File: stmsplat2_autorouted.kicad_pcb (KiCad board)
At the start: 2 copper layers, 100 x 100 mm, 113 parts, among them J1 C11_2X36, J10 Conn_01x03_Male, J11 Conn_01x02_Male, J12 Conn_01x04_Male, J13 Conn_01x04_Male, J14 Conn_01x02, J15 Conn_01x02, J16 Screw_Terminal_01x03, J17 Screw_Terminal_01x02, J2 C12_2X36, J3 Conn_01x04_Male, J4 Conn_01x04_Male, J5 Conn_Coaxial, J6 Conn_01x04_Male, J7 Conn_01x04_Male, J8 Conn_01x04_Male, J9 Conn_01x03_Male, Q1 BSS138LT1G, U1 ublox_chinese_PCB_module, U10 XCVR_E30-400M20S (Si4463), U11 3115_module, U2 ESP-C3-13U, U3 SST25VF032B, U4 48L512-48LM01, U5 Opamp_Quad_MCP6024, U6 E180-ZG120A, U7 AZ1084C, U8 MCP6S93-X_UN, U9 DS2485

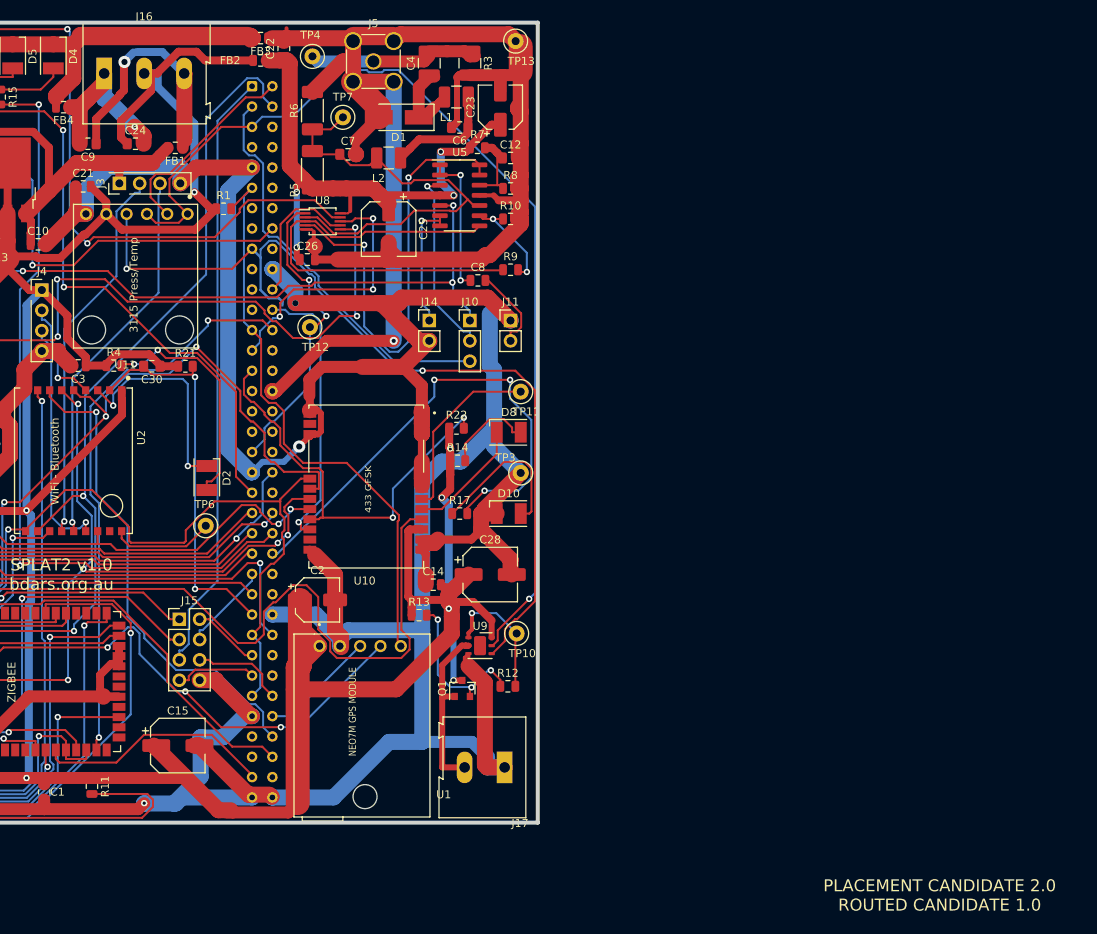
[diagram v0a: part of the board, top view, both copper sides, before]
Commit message: placement candidate 2 with routed candidate 1.0
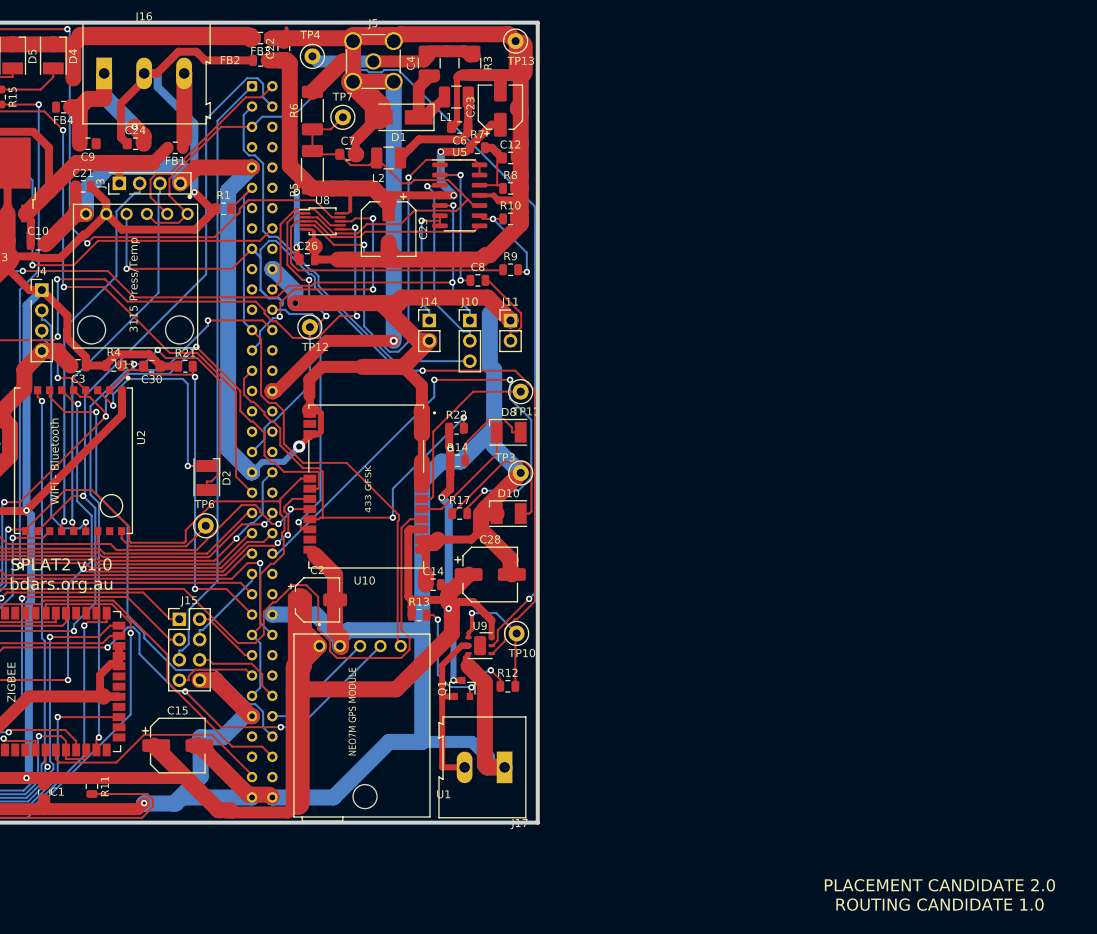
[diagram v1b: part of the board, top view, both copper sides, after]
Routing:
- net /RAW5V: track 29.4 -> 9.40 mm, vias 1 -> 0
- net GND: track 882.5 -> 878.0 mm
- net /RAWGND: track 22.2 -> 23.3 mm
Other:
- board text added: "PLACEMENT CANDIDATE 2.0 ROUTING CANDIDATE 1.0"
- board text removed: "PLACEMENT CANDIDATE 2.0 ROUTED CANDIDATE 1.0"
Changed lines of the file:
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@@
     (thickness 1.6)
     (drawings 16)
-    (tracks 2275)
+    (tracks 2261)
     (zones 0)
     (modules 113)
@@
   (page A4)
   (layers
-    (0 F.Cu signal)
-    (31 B.Cu signal)
+    (0 F.Cu signal hide)
+    (31 B.Cu signal hide)
     (33 F.Adhes user)
     (35 F.Paste user)
@@
   )
   (setup
-    (last_trace_width 1)
+    (last_trace_width 0.25)
     (user_trace_width 0.25)
     (user_trace_width 0.3)
@@
     (effects (font (size 1.5 1.5) (thickness 0.3)))
   )
-  (gr_text "PLACEMENT CANDIDATE 2.0\nROUTED CANDIDATE 1.0" (at 202.2348 174.7266) (layer F.SilkS)
+  (gr_text "PLACEMENT CANDIDATE 2.0\nROUTING CANDIDATE 1.0" (at 202.2348 174.7266) (layer F.SilkS)
     (effects (font (size 1.5 1.5) (thickness 0.3)))
   )
@@
   (via (at 122.174 118.618) (size 1.524) (drill 0.762) (layers F.Cu B.Cu) (net 26))
   (via (at 121.693 100.698) (size 0.8) (drill 0.762) (layers F.Cu B.Cu) (net 26))
-  (segment (start 91.7725 76.2) (end 91.7725 75.0085) (width 1) (layer F.Cu) (net 26))
-  (segment (start 91.7725 74.7834) (end 93.9403 72.6156) (width 2) (layer F.Cu) (net 26))
-  (segment (start 91.7725 75.0085) (end 91.7725 74.7834) (width 2) (layer F.Cu) (net 26))
   (segment (start 75.946 128.1176) (end 75.946 128.016) (width 0.75) (layer F.Cu) (net 27))
   (segment (start 71.915 133.35) (end 75.184 133.35) (width 0.75) (layer F.Cu) (net 27))
@@
   (segment (start 109.1793 91.5112) (end 100.0262 91.5112) (width 1) (layer F.Cu) (net 117))
   (segment (start 100.0262 91.5112) (end 98.06 89.545) (width 1) (layer F.Cu) (net 117))
+  (segment (start 103.6352 71.9836) (end 99.895 75.7238) (width 1) (layer F.Cu) (net 117))
+  (segment (start 99.895 75.7238) (end 99.895 79.99) (width 1) (layer F.Cu) (net 117))
+  (segment (start 99.895 79.99) (end 100.677 80.772) (width 1) (layer F.Cu) (net 117))
   (segment (start 103.6352 71.9836) (end 104.4803 71.9836) (width 1) (layer F.Cu) (net 117))
   (segment (start 102.79 71.9836) (end 103.6352 71.9836) (width 1) (layer F.Cu) (net 117))
@@
   (via (at 141.048 118.849) (size 0.8) (drill 0.508) (layers F.Cu B.Cu) (net 117))
   (via (at 141.46 147.86) (size 0.8) (drill 0.508) (layers F.Cu B.Cu) (net 117))
-  (segment (start 99.895 79.99) (end 100.677 80.772) (width 1) (layer F.Cu) (net 117))
-  (segment (start 99.895 77.905) (end 99.895 79.99) (width 1) (layer F.Cu) (net 117))
-  (segment (start 103.6352 74.1648) (end 99.895 77.905) (width 1) (layer F.Cu) (net 117))
-  (segment (start 103.6352 71.9836) (end 103.6352 74.1648) (width 1) (layer F.Cu) (net 117))
   (segment (start 87.2601 133.4961) (end 87.5601 133.1961) (width 0.25) (layer F.Cu) (net 118))
   (segment (start 87.5601 133.1961) (end 95.5016 133.1961) (width 0.25) (layer F.Cu) (net 118))
@@
   (segment (start 107.618 81.28) (end 107.618 80.4695) (width 1.5) (layer F.Cu) (net 183))
   (segment (start 107.618 80.4695) (end 107.823 80.264) (width 1.5) (layer F.Cu) (net 183))
-  (segment (start 96.792 77.661602) (end 99.74001 74.713592) (width 1) (layer F.Cu) (net 183))
-  (segment (start 96.792 80.772) (end 96.792 77.661602) (width 1) (layer F.Cu) (net 183))
-  (segment (start 101.893743 69.30359) (end 105.05409 69.30359) (width 1) (layer B.Cu) (net 183))
-  (segment (start 100.569708 70.246625) (end 101.449243 69.36709) (width 1) (layer B.Cu) (net 183))
-  (segment (start 105.05409 69.30359) (end 107.823 72.0725) (width 1) (layer B.Cu) (net 183))
-  (segment (start 99.74001 74.713592) (end 99.74001 74.63099) (width 1) (layer F.Cu) (net 183))
-  (segment (start 99.74001 74.63099) (end 100.2665 74.1045) (width 1) (layer F.Cu) (net 183))
-  (via (at 100.33 70.5485) (size 1.524) (drill 0.762) (layers F.Cu B.Cu) (net 183))
-  (segment (start 100.2665 70.612) (end 100.33 70.5485) (width 1) (layer F.Cu) (net 183))
-  (segment (start 100.2665 74.1045) (end 100.2665 70.612) (width 1) (layer F.Cu) (net 183))
   (segment (start 94.742 76.2) (end 94.742 80.772) (width 2) (layer F.Cu) (net 184))
   (segment (start 97.79 71.9836) (end 97.79 75.1639) (width 2) (layer B.Cu) (net 184))
@@
   (segment (start 97.79 75.1639) (end 98.1118 75.1639) (width 2) (layer B.Cu) (net 184))
   (segment (start 98.1118 75.1639) (end 101.5953 78.6474) (width 2) (layer B.Cu) (net 184))
+  (segment (start 97.79 71.9836) (end 97.79 75.1639) (width 2) (layer F.Cu) (net 184))
   (segment (start 94.742 76.2) (end 93.6475 76.2) (width 2) (layer F.Cu) (net 184))
-  (via (at 101.5953 78.6474) (size 0.8) (layers F.Cu B.Cu) (net 184))
+  (segment (start 97.79 75.1639) (end 95.7781 75.1639) (width 2) (layer F.Cu) (net 184))
   (segment (start 95.7781 75.1639) (end 94.742 76.2) (width 2) (layer F.Cu) (net 184))
-  (segment (start 97.79 73.152) (end 95.7781 75.1639) (width 2) (layer F.Cu) (net 184))
-  (segment (start 97.79 71.9836) (end 97.79 73.152) (width 2) (layer F.Cu) (net 184))
+  (via (at 101.5953 78.6474) (size 0.8) (layers F.Cu B.Cu) (net 184))
   (segment (start 80.391 113.3875) (end 81.4648 112.3137) (width 0.25) (layer F.Cu) (net 185))
   (segment (start 81.4648 112.3137) (end 81.4648 110.5388) (width 0.25) (layer F.Cu) (net 185))
